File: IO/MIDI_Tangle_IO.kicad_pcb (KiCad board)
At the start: 2 copper layers, 40 x 99.5 mm, 54 parts, among them J1 Conn_01x08_Male, J10 AudioJack2, J11 AudioJack2, J12 AudioJack2, J13 AudioJack2, J14 AudioJack2, J15 AudioJack2, J16 AudioJack2, J17 AudioJack2, J18 AudioJack2, J19 AudioJack2, J2 Conn_01x08_Male, J20 AudioJack2, J3 Conn_01x08_Male, J4 Conn_01x08_Male, J5 AudioJack2, J6 AudioJack2, J7 AudioJack2, J8 AudioJack2, J9 AudioJack2, SW1 SW_SPST, SW2 SW_SPST, SW3 SW_SPST, SW4 SW_SPST, SW5 SW_SPST, SW6 SW_SPST, SW7 SW_SPST, SW8 SW_SPST

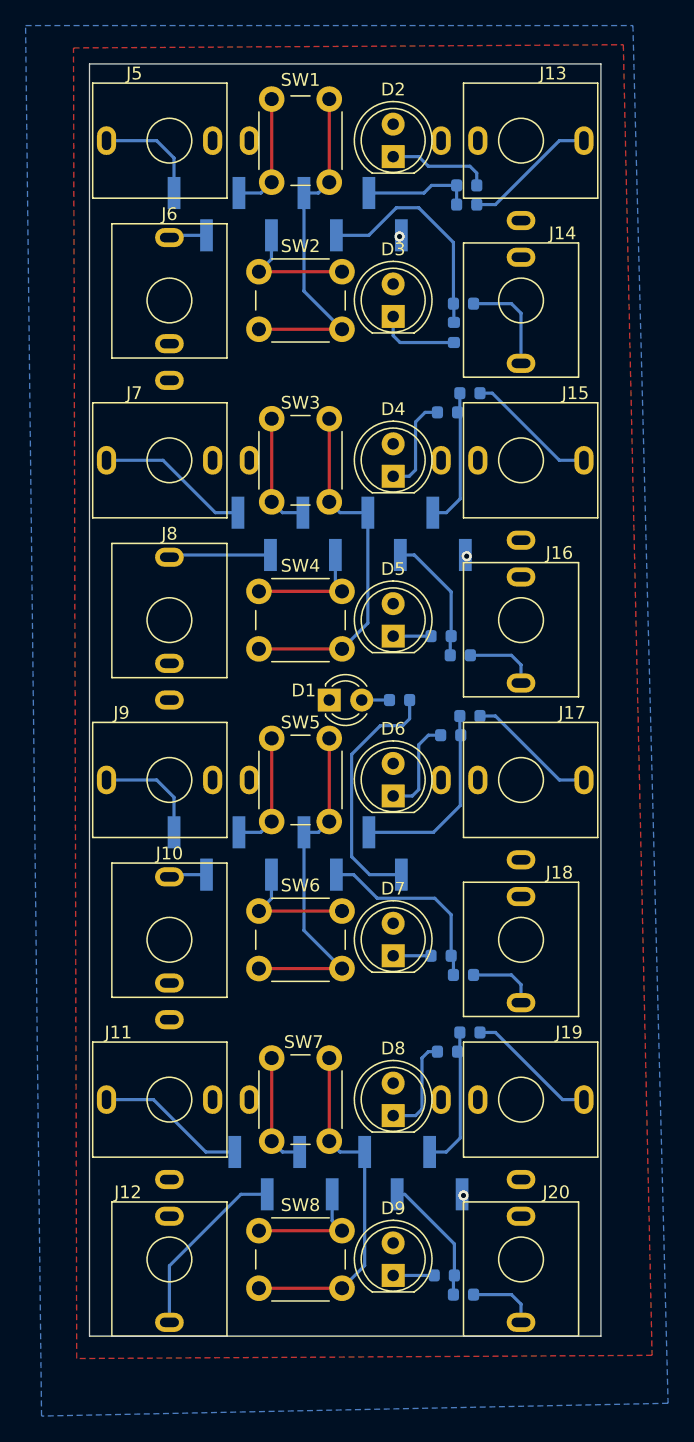
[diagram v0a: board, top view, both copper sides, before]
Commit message: Add custom footprints and symbols
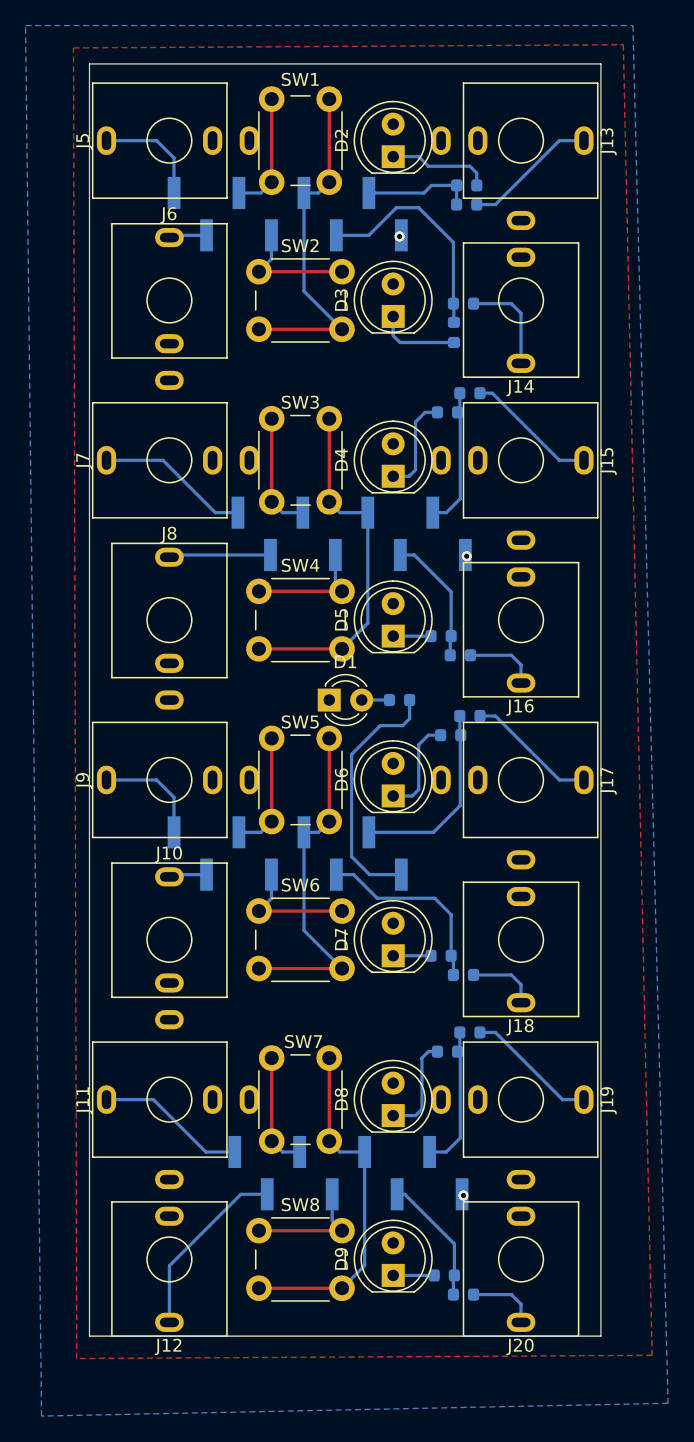
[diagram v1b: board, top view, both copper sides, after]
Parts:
- D1: footprint LED_THT:LED_D3.0mm -> Custom_FP:LED_D3.0mm_NoCourtyard
- D2, D3, D4, D5, D6, D7, D8, D9: footprint LED_THT:LED_D5.0mm_FlatTop -> Custom_FP:LED_D5.0mm_FlatTop_NoCourtyard
- J10, J11, J12, J13, J14, J15, J16, J17, J18, J19, J20, J5, J6, J7, J8, J9: footprint CustomLib:PJ398SM -> Custom_FP:PJ398SM

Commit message: Add new bi-color LEDs
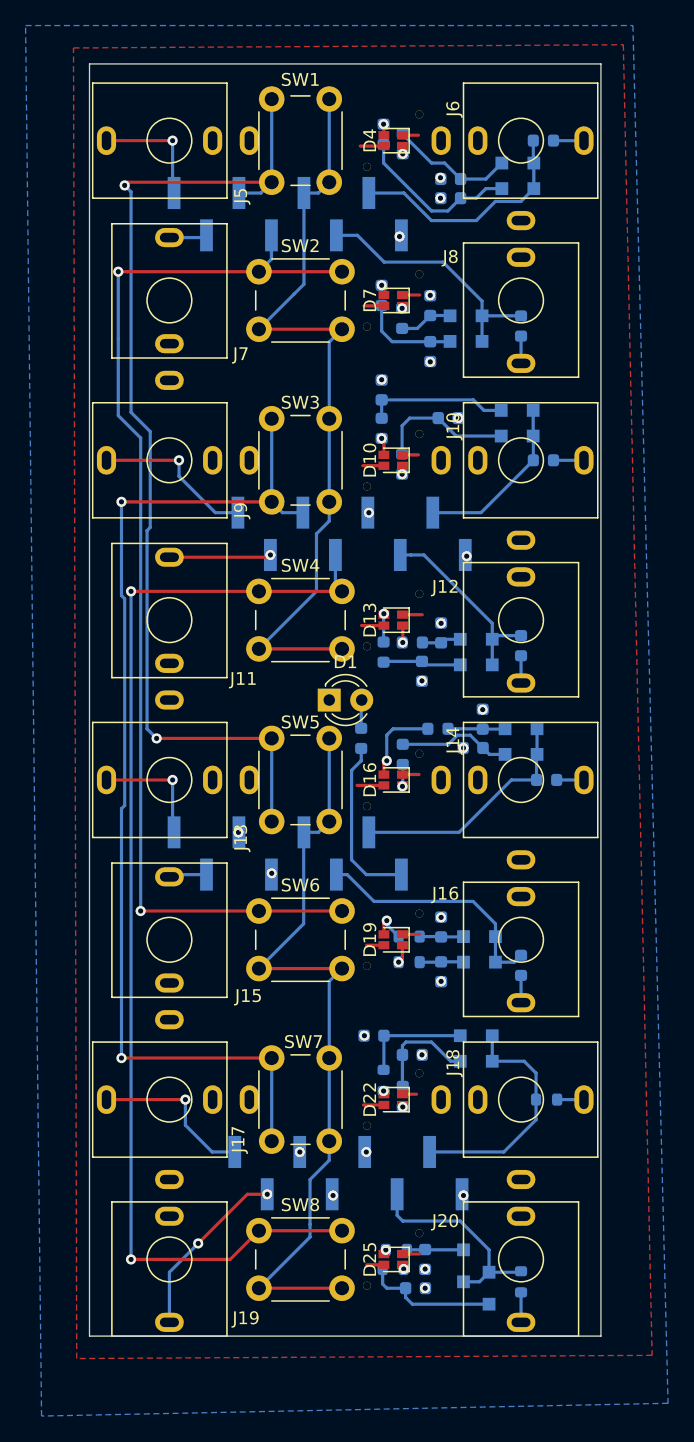
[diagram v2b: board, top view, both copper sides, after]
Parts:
- added C1: 100nF, Capacitor_SMD:C_0603_1608Metric, B.Cu at (78.0, 61.0)
- added C10: 100nF, Capacitor_SMD:C_0603_1608Metric, B.Cu at (79.8, 104.0)
- added C11: 100nF, Capacitor_SMD:C_0603_1608Metric, B.Cu at (77.2, 118.0)
- added C12: 100nF, Capacitor_SMD:C_0603_1608Metric, B.Cu at (77.2, 121.5)
- added C13: 100nF, Capacitor_SMD:C_0603_1608Metric, B.Cu at (72.0, 126.5)
- added C14: 100nF, Capacitor_SMD:C_0603_1608Metric, B.Cu at (75.0, 128.0)
- added C15: 100nF, Capacitor_SMD:C_0603_1608Metric, B.Cu at (76.0, 144.0)
- added C16: 100nF, Capacitor_SMD:C_0603_1608Metric, B.Cu at (75.2, 146.2)
- added C2: 100nF, Capacitor_SMD:C_0603_1608Metric, B.Cu at (78.0, 59.5)
- added C3: 100nF, Capacitor_SMD:C_0603_1608Metric, B.Cu at (76.4, 73.0)
- added C4: 100nF, Capacitor_SMD:C_0603_1608Metric, B.Cu at (76.4, 69.4)
- added C5: 100nF, Capacitor_SMD:C_0603_1608Metric, B.Cu at (72.6, 76.0)
- added C6: 100nF, Capacitor_SMD:C_0603_1608Metric, B.Cu at (77.8, 78.2)
- added C7: 100nF, Capacitor_SMD:C_0603_1608Metric, B.Cu at (75.8, 98.0)
- added C8: 100nF, Capacitor_SMD:C_0603_1608Metric, B.Cu at (77.2, 95.0)
- added C9: 100nF, Capacitor_SMD:C_0603_1608Metric, B.Cu at (80.5, 101.8)
- added D10: LTST-C195TGKRKT, Custom_FP:LED_LiteOn_LTST-C195TGKRKT, F.Cu at (73.5, 81.5)
- added D11: SD103, Diode_SMD:D_SOD-323_HandSoldering, B.Cu at (80.0, 97.5)
- added D12: SD103, Diode_SMD:D_SOD-323_HandSoldering, B.Cu at (80.0, 95.5)
- added D13: LTST-C195TGKRKT, Custom_FP:LED_LiteOn_LTST-C195TGKRKT, F.Cu at (73.5, 94.0)
- added D14: SD103, Diode_SMD:D_SOD-323_HandSoldering, B.Cu at (83.5, 102.5)
- added D15: SD103, Diode_SMD:D_SOD-323_HandSoldering, B.Cu at (83.5, 104.5)
- added D16: LTST-C195TGKRKT, Custom_FP:LED_LiteOn_LTST-C195TGKRKT, F.Cu at (73.5, 106.5)
- added D17: SD103, Diode_SMD:D_SOD-323_HandSoldering, B.Cu at (80.2, 118.8)
- added D18: SD103, Diode_SMD:D_SOD-323_HandSoldering, B.Cu at (80.2, 120.8)
- added D19: LTST-C195TGKRKT, Custom_FP:LED_LiteOn_LTST-C195TGKRKT, F.Cu at (73.5, 119.0)
- added D20: SD103, Diode_SMD:D_SOD-323_HandSoldering, B.Cu at (80.0, 126.5)
- added D21: SD103, Diode_SMD:D_SOD-323_HandSoldering, B.Cu at (80.0, 128.5)
- added D22: LTST-C195TGKRKT, Custom_FP:LED_LiteOn_LTST-C195TGKRKT, F.Cu at (73.5, 131.5)
- added D23: SD103, Diode_SMD:D_SOD-323_HandSoldering, B.Cu at (79.0, 144.5)
- added D24: SD103, Diode_SMD:D_SOD-323_HandSoldering, B.Cu at (81.0, 146.2)
- added D25: LTST-C195TGKRKT, Custom_FP:LED_LiteOn_LTST-C195TGKRKT, F.Cu at (73.5, 144.0)
- added H1: LightPipe, Custom_FP:VLP-LightPipes, F.Cu at (73.5, 56.5)
- added H2: LightPipe, Custom_FP:VLP-LightPipes, F.Cu at (73.5, 69.0)
- added H3: LightPipe, Custom_FP:VLP-LightPipes, F.Cu at (73.5, 81.5)
- added H4: LightPipe, Custom_FP:VLP-LightPipes, F.Cu at (73.5, 94.0)
- added H5: LightPipe, Custom_FP:VLP-LightPipes, F.Cu at (73.5, 106.5)
- added H6: LightPipe, Custom_FP:VLP-LightPipes, F.Cu at (73.5, 119.0)
- added H7: LightPipe, Custom_FP:VLP-LightPipes, F.Cu at (73.5, 131.5)
- added H8: LightPipe, Custom_FP:VLP-LightPipes, F.Cu at (73.5, 144.0)
- added R18: 680, Resistor_SMD:R_0603_1608Metric, B.Cu at (74.8, 118.8)
- added R19: 1k, Resistor_SMD:R_0603_1608Metric, B.Cu at (74.8, 120.8)
- added R20: 1k, Resistor_SMD:R_0603_1608Metric, B.Cu at (85.5, 131.5)
- added R21: 680, Resistor_SMD:R_0603_1608Metric, B.Cu at (72.8, 130.0)
- added R22: 1k, Resistor_SMD:R_0603_1608Metric, B.Cu at (74.2, 131.2)
- added R23: 1k, Resistor_SMD:R_0603_1608Metric, B.Cu at (83.5, 145.8)
- added R24: 680, Resistor_SMD:R_0603_1608Metric, B.Cu at (73.8, 143.2)
- added R25: 1k, Resistor_SMD:R_0603_1608Metric, B.Cu at (73.5, 144.8)
- D2, D3, D5, D6, D8, D9: value LED_RG -> SD103; footprint Custom_FP:LED_D5.0mm_FlatTop_NoCourtyard -> Diode_SMD:D_SOD-323_HandSoldering; moved to B.Cu
- D4, D7: value LED_RG -> LTST-C195TGKRKT; footprint Custom_FP:LED_D5.0mm_FlatTop_NoCourtyard -> Custom_FP:LED_LiteOn_LTST-C195TGKRKT
- J10, J11, J12, J13, J14, J15, J16, J17, J18, J19, J20, J5, J6, J7, J8, J9: value AudioJack2 -> AudioJack2_SwitchT
- R12, R15, R3, R6, R9: value 1k -> 680
- moved D9 66.4 mm to (83.2, 79.6), turned to 180 degrees
- moved J12 57.1 mm to (83.5, 94.0)
- moved J13 57.1 mm to (56.0, 106.5), turned to 90 degrees
- moved D8 56.0 mm to (83.2, 77.6), turned to 0 degrees
- moved D7 51.2 mm to (73.5, 69.0)
- moved J10 46.5 mm to (83.5, 81.5), turned to 270 degrees
- moved J15 46.5 mm to (56.0, 119.0), turned to 0 degrees
- moved R16 42.5 mm to (74.2, 104.5), turned to 270 degrees
- moved D6 38.0 mm to (79.2, 70.2), turned to 180 degrees
- moved J11 37.5 mm to (56.0, 94.0), turned to 0 degrees
- moved J14 37.5 mm to (83.5, 106.5), turned to 270 degrees
- moved J17 37.2 mm to (56.0, 131.5), turned to 90 degrees
- moved J8 37.2 mm to (83.5, 69.0), turned to 180 degrees
- moved J19 30.2 mm to (56.0, 144.0), turned to 180 degrees
- moved J6 30.2 mm to (83.5, 56.5), turned to 270 degrees
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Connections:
- D2 pad 1: Net-(D2-Pad1) -> Net-(C1-Pad1)
- D2 pad 2: GND -> JackO1
- D3 pad 1: Net-(D3-Pad1) -> JackO1
- D3 pad 2: GND -> Net-(C2-Pad1)
- D5 pad 1: Net-(D5-Pad1) -> Net-(C3-Pad1)
- D5 pad 2: GND -> JackO2
- D6 pad 1: Net-(D6-Pad1) -> JackO2
- D6 pad 2: GND -> Net-(C4-Pad1)
- D8 pad 1: Net-(D8-Pad1) -> Net-(C5-Pad1)
- D8 pad 2: GND -> JackO3
- D9 pad 1: Net-(D9-Pad1) -> JackO3
- D9 pad 2: GND -> Net-(C6-Pad1)
- J1 pad 5: ButtSel1 -> ButtSelX
- J10 pad T: JackI6 -> Net-(J10-PadT)
- J11 pad T: JackI7 -> JackI4
- J11 pad TN: (no net) -> GND
- J12 pad T: JackI8 -> Net-(J12-PadT)
- J13 pad T: Net-(J13-PadT) -> JackI5
- J13 pad TN: (no net) -> GND
- J15 pad T: Net-(J15-PadT) -> JackI6
- J15 pad TN: (no net) -> GND
- J17 pad T: Net-(J17-PadT) -> JackI7
- J17 pad TN: (no net) -> GND
- J19 pad T: Net-(J19-PadT) -> JackI8
- J19 pad TN: (no net) -> GND
- J2 pad 5: ButtSel2 -> GND
- J3 pad 3: Butt5 -> GND
- J3 pad 4: Butt6 -> GND
- J3 pad 5: ButtSel3 -> ButtSelY
- J4 pad 3: Butt7 -> GND
- J4 pad 4: Butt8 -> GND
- J4 pad 5: ButtSel4 -> GND
- J5 pad TN: (no net) -> GND
- J6 pad T: JackI2 -> Net-(J6-PadT)
- J7 pad T: JackI3 -> JackI2
- J7 pad TN: (no net) -> GND
- J8 pad T: JackI4 -> Net-(J8-PadT)
- J9 pad T: JackI5 -> JackI3
- J9 pad TN: (no net) -> GND
- R10 pad 1: Net-(J17-PadT) -> Net-(C6-Pad1)
- R10 pad 2: JackO5 -> Net-(D10-Pad4)
- R11 pad 1: Net-(D6-Pad1) -> JackO4
- R11 pad 2: JackO5 -> Net-(J12-PadT)
- R12 pad 1: Net-(J18-PadT) -> Net-(D13-Pad1)
- R12 pad 2: JackO6 -> Net-(C7-Pad1)
- R13 pad 1: Net-(D7-Pad1) -> Net-(C8-Pad1)
- R13 pad 2: JackO6 -> Net-(D13-Pad4)
- R14 pad 1: Net-(J19-PadT) -> JackO5
- R14 pad 2: JackO7 -> Net-(J14-PadT)
- R15 pad 1: Net-(D8-Pad1) -> Net-(D16-Pad1)
- R15 pad 2: JackO7 -> Net-(C9-Pad1)
- R16 pad 1: Net-(J20-PadT) -> Net-(C10-Pad1)
- R16 pad 2: JackO8 -> Net-(D16-Pad4)
- R17 pad 1: Net-(D9-Pad1) -> JackO6
- R17 pad 2: JackO8 -> Net-(J16-PadT)
- R2 pad 1: Net-(J13-PadT) -> JackO1
- R2 pad 2: JackO1 -> Net-(J6-PadT)
- R3 pad 1: Net-(D2-Pad1) -> Net-(D4-Pad1)
- R3 pad 2: JackO1 -> Net-(C1-Pad1)
- R4 pad 1: Net-(J14-PadT) -> Net-(C2-Pad1)
- R4 pad 2: JackO2 -> Net-(D4-Pad4)
- R5 pad 1: Net-(D3-Pad1) -> JackO2
- R5 pad 2: JackO2 -> Net-(J8-PadT)
- R6 pad 1: Net-(J15-PadT) -> Net-(D7-Pad1)
- R6 pad 2: JackO3 -> Net-(C3-Pad1)
- R7 pad 1: Net-(D4-Pad1) -> Net-(C4-Pad1)
- R7 pad 2: JackO3 -> Net-(D7-Pad4)
- R8 pad 1: Net-(J16-PadT) -> JackO3
- R8 pad 2: JackO4 -> Net-(J10-PadT)
- R9 pad 1: Net-(D5-Pad1) -> Net-(D10-Pad1)
- R9 pad 2: JackO4 -> Net-(C5-Pad1)
- SW1 pad 2: ButtSel1 -> ButtSelX
- SW2 pad 2: ButtSel1 -> ButtSelX
- SW3 pad 2: ButtSel2 -> ButtSelX
- SW4 pad 2: ButtSel2 -> ButtSelX
- SW5 pad 1: Butt5 -> Butt1
- SW5 pad 2: ButtSel3 -> ButtSelY
- SW6 pad 1: Butt6 -> Butt2
- SW6 pad 2: ButtSel3 -> ButtSelY
- SW7 pad 1: Butt7 -> Butt3
- SW7 pad 2: ButtSel4 -> ButtSelY
- SW8 pad 1: Butt8 -> Butt4
- SW8 pad 2: ButtSel4 -> ButtSelY
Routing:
- net Butt4: track 9.56 -> 89.2 mm, vias 0 -> 2
- net Butt2: track 9.75 -> 87.2 mm, vias 0 -> 2
- net Butt3: track 9.29 -> 83.0 mm, vias 0 -> 2
- net Butt1: track 9.41 -> 81.0 mm, vias 0 -> 2
- net ButtSelY: track 0.00 -> 61.6 mm
- net ButtSelX: track 0.00 -> 61.6 mm
- net ButtSel2: track 27.9 -> 0.00 mm
- net ButtSel4: track 27.5 -> 0.00 mm
- net ButtSel3: track 27.2 -> 0.00 mm
- net ButtSel1: track 27.2 -> 0.00 mm
- net GND: track 0.18 -> 23.9 mm, vias 3 -> 25
- net Net-(C1-Pad1): track 0.00 -> 13.0 mm
- net Net-(C5-Pad1): track 0.00 -> 11.1 mm
- net Net-(C6-Pad1): track 0.00 -> 10.8 mm
- net Net-(C16-Pad1): track 0.00 -> 10.6 mm
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
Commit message: Fix IO drc
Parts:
- moved J3 0.21 mm to (65.4, 112.4)
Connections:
- J10 pad TN: (no net) -> unconnected-(J10-PadTN)
- J12 pad TN: (no net) -> unconnected-(J12-PadTN)
- J14 pad TN: (no net) -> unconnected-(J14-PadTN)
- J16 pad TN: (no net) -> unconnected-(J16-PadTN)
- J18 pad TN: (no net) -> unconnected-(J18-PadTN)
- J20 pad TN: (no net) -> unconnected-(J20-PadTN)
- J6 pad TN: (no net) -> unconnected-(J6-PadTN)
- J8 pad TN: (no net) -> unconnected-(J8-PadTN)
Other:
- net class Default removed

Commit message: Update PCB layout
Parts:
- moved R1 4.00 mm to (73.8, 100.4), turned to 180 degrees
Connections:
- J1 pad 3: Butt1 -> JackO1
- J1 pad 4: Butt2 -> JackO2
- J1 pad 5: ButtSelX -> Butt1
- J1 pad 6: JackO2 -> Butt2
- J1 pad 7: JackO1 -> GND
- J2 pad 5: GND -> JackO4
- J2 pad 6: JackO4 -> ButtSelX
- J2 pad 8: GND -> Net-(J2-Pin_8)
- J3 pad 8: Net-(J3-Pin_8) -> GND
- R1 pad 1: Net-(J3-Pin_8) -> Net-(J2-Pin_8)
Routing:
- net Net-(J2-Pin_8): track 0.00 -> 30.9 mm, vias 0 -> 4
- net JackO1: track 18.6 -> 46.1 mm
- net Net-(J3-Pin_8): track 13.4 -> 0.00 mm
- net JackO2: track 19.7 -> 28.8 mm, vias 0 -> 2
- net ButtSelX: track 61.6 -> 70.4 mm, vias 0 -> 1
- net JackO4: track 15.0 -> 21.2 mm, vias 0 -> 2
- net GND: vias 25 -> 24
